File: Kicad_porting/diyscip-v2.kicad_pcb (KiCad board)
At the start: 2 copper layers, 86.4 x 24.1 mm, 30 parts, among them IC1 CD4051BE, IC2 CD4051BE, IC3 SN74HC595N, IC4 SN74HC595N, J1 Conn_01x05_Male, J3 Conn_01x05_Male, Q1 BSS138, Q2 BSS138, Q3 BSS138, U1 AMS1117-3.3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

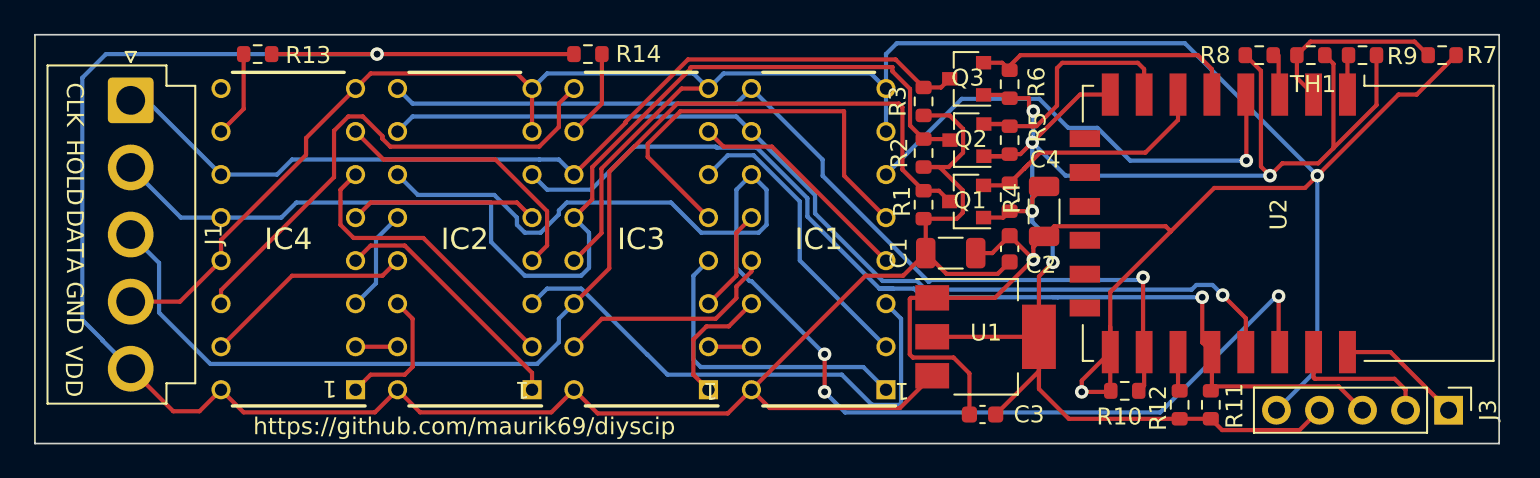
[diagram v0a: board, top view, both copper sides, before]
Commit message: gerber with thermal copper
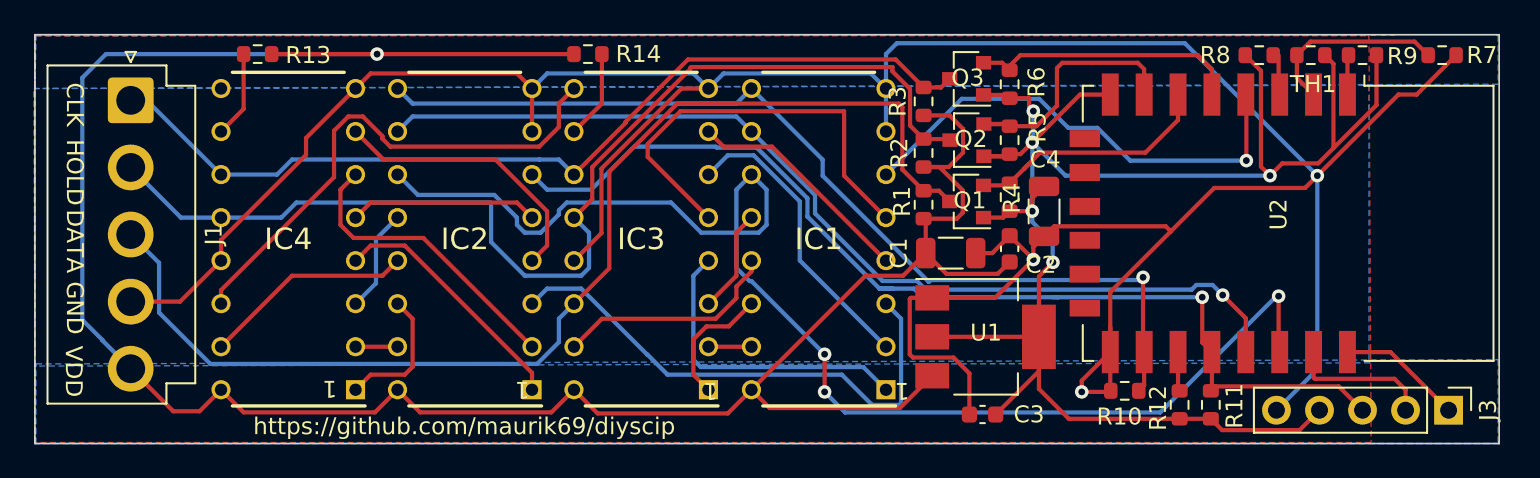
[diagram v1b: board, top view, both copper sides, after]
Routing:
- added copper zone on B.Cu, net GND
- added copper zone on F.Cu, net GND

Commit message: Correzione errore scritta connettore programmazione.
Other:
- board text added: "+3.3"
- board text removed: "3.3V"
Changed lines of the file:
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@@
   )
   (layers
-    (0 F.Cu signal)
-    (31 B.Cu signal)
+    (0 F.Cu signal hide)
+    (31 B.Cu signal hide)
     (32 B.Adhes user)
     (33 F.Adhes user)
@@
     (44 Edge.Cuts user)
     (45 Margin user)
-    (46 B.CrtYd user hide)
+    (46 B.CrtYd user)
     (47 F.CrtYd user)
-    (48 B.Fab user hide)
+    (48 B.Fab user)
     (49 F.Fab user hide)
   )
@@
       (effects (font (size 1 1) (thickness 0.15)))
     )
-    (fp_text value Conn_01x05_Male (at 0 12.49 90) (layer F.Fab)
+    (fp_text value Conn_01x05_Male (at 2.159 4.953 180) (layer F.Fab)
       (effects (font (size 1 1) (thickness 0.15)))
     )
@@
       (effects (font (size 1 1) (thickness 0.15)))
     )
-    (fp_text value "Thermistor NTC 10K" (at 0 1.43) (layer F.Fab)
+    (fp_text value "Thermistor NTC 10K" (at -0.191 3.1115) (layer F.Fab)
       (effects (font (size 1 1) (thickness 0.15)))
     )
@@
       (effects (font (size 1 1) (thickness 0.15)))
     )
-    (fp_text value 10k (at 0 1.43) (layer F.Fab)
+    (fp_text value 10k (at 0.1275 1.651) (layer F.Fab)
       (effects (font (size 1 1) (thickness 0.15)))
     )
@@
       (effects (font (size 1 1) (thickness 0.15)))
     )
-    (fp_text value ESP-12E (at -0.06 -12.78 90) (layer F.Fab)
+    (fp_text value ESP-12E (at 0.615 2.341 90) (layer F.Fab)
       (effects (font (size 1 1) (thickness 0.15)))
     )
@@
       (effects (font (size 1 1) (thickness 0.15)))
     )
-    (fp_text value 10K (at 0 1.43) (layer F.Fab)
+    (fp_text value 10K (at -0.1275 -1.778) (layer F.Fab)
       (effects (font (size 1 1) (thickness 0.15)))
     )
@@
       (effects (font (size 1 1) (thickness 0.15)))
     )
-    (fp_text value 10K (at 0 1.43) (layer F.Fab)
+    (fp_text value 10K (at 0.1275 1.8415) (layer F.Fab)
       (effects (font (size 1 1) (thickness 0.15)))
     )
@@
       (effects (font (size 1 1) (thickness 0.15)))
     )
-    (fp_text value 100nF (at 0 1.43) (layer F.Fab)
+    (fp_text value 100nF (at -0.013 -0.127) (layer F.Fab)
       (effects (font (size 1 1) (thickness 0.15)))
     )
@@
       (effects (font (size 1 1) (thickness 0.15)))
     )
-    (fp_text value AMS1117-3.3 (at 0 4.5) (layer F.Fab)
+    (fp_text value AMS1117-3.3 (at 0.2155 -0.113) (layer F.Fab)
       (effects (font (size 1 1) (thickness 0.15)))
     )
@@
       (effects (font (size 1 1) (thickness 0.15)))
     )
-    (fp_text value BSS138 (at 0 2.5) (layer F.Fab)
+    (fp_text value BSS138 (at 0.143 0.061) (layer F.Fab)
       (effects (font (size 1 1) (thickness 0.15)))
     )
@@
       (effects (font (size 1 1) (thickness 0.15)))
     )
-    (fp_text value 100nF (at 0 1.43 90) (layer F.Fab)
+    (fp_text value 100nF (at -0.9525 1.27 180) (layer F.Fab)
       (effects (font (size 1 1) (thickness 0.15)))
     )
@@
     (fp_line (start -1.6 -0.8) (end 1.6 -0.8) (layer F.Fab) (width 0.1))
     (fp_line (start -1.6 0.8) (end -1.6 -0.8) (layer F.Fab) (width 0.1))
-    (fp_text user %R (at 0 0) (layer F.Fab)
+    (fp_text user %R (at 0.049 0.0635) (layer F.Fab)
       (effects (font (size 0.8 0.8) (thickness 0.12)))
     )
@@
     (effects (font (size 1 1) (thickness 0.15)))
   )
-  (gr_text 3.3V (at 185.928 102.616) (layer B.SilkS)
+  (gr_text GND (at 187.1345 102.0445 270) (layer B.SilkS)
     (effects (font (size 1 1) (thickness 0.15)) (justify mirror))
   )
-  (gr_text GND (at 189.23 102.616) (layer B.SilkS)
+  (gr_text +3.3 (at 189.738 101.7905 270) (layer B.SilkS)
     (effects (font (size 1 1) (thickness 0.15)) (justify mirror))
   )
-  (gr_text G0 (at 192.3415 102.616) (layer B.SilkS)
+  (gr_text G0 (at 192.278 102.5525 270) (layer B.SilkS)
     (effects (font (size 1 1) (thickness 0.15)) (justify mirror))
   )
-  (gr_text RX (at 194.945 102.616) (layer B.SilkS)
+  (gr_text RX (at 194.7545 102.616 270) (layer B.SilkS)
     (effects (font (size 1 1) (thickness 0.15)) (justify mirror))
   )
-  (gr_text TX (at 197.485 102.6795) (layer B.SilkS)
+  (gr_text TX (at 197.358 102.5525 270) (layer B.SilkS)
     (effects (font (size 1 1) (thickness 0.15)) (justify mirror))
   )

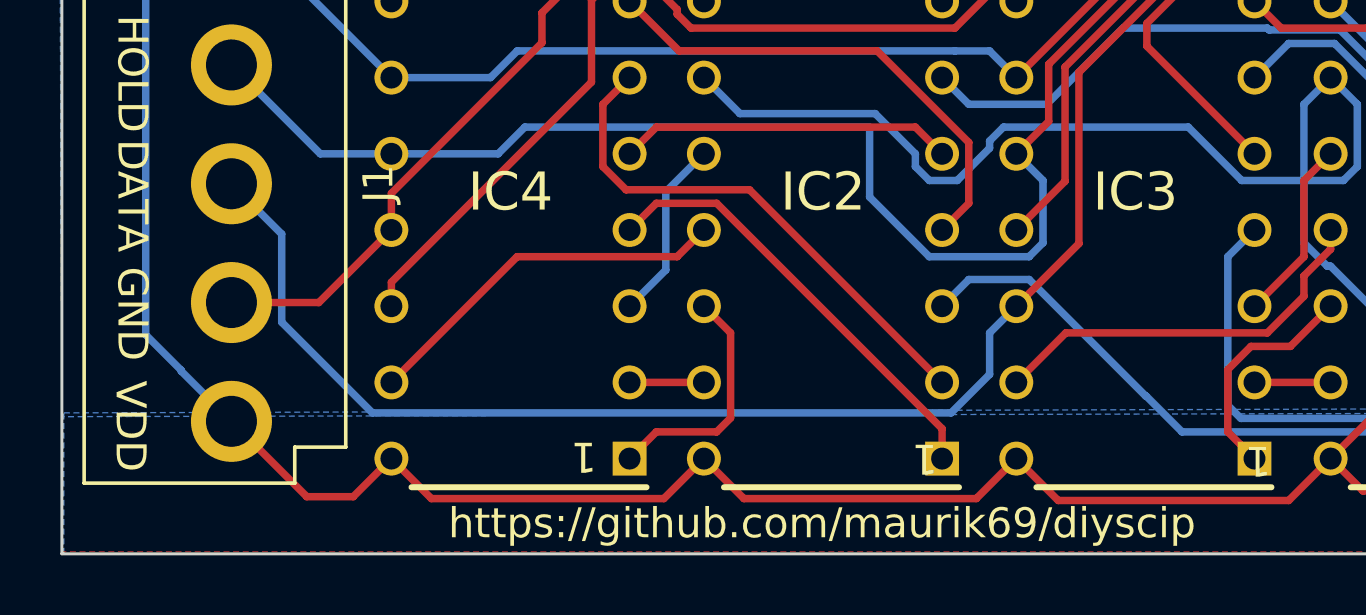
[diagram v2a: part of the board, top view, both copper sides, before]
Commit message: Aggiunta resistenza "dimenticata" su segnale DATA
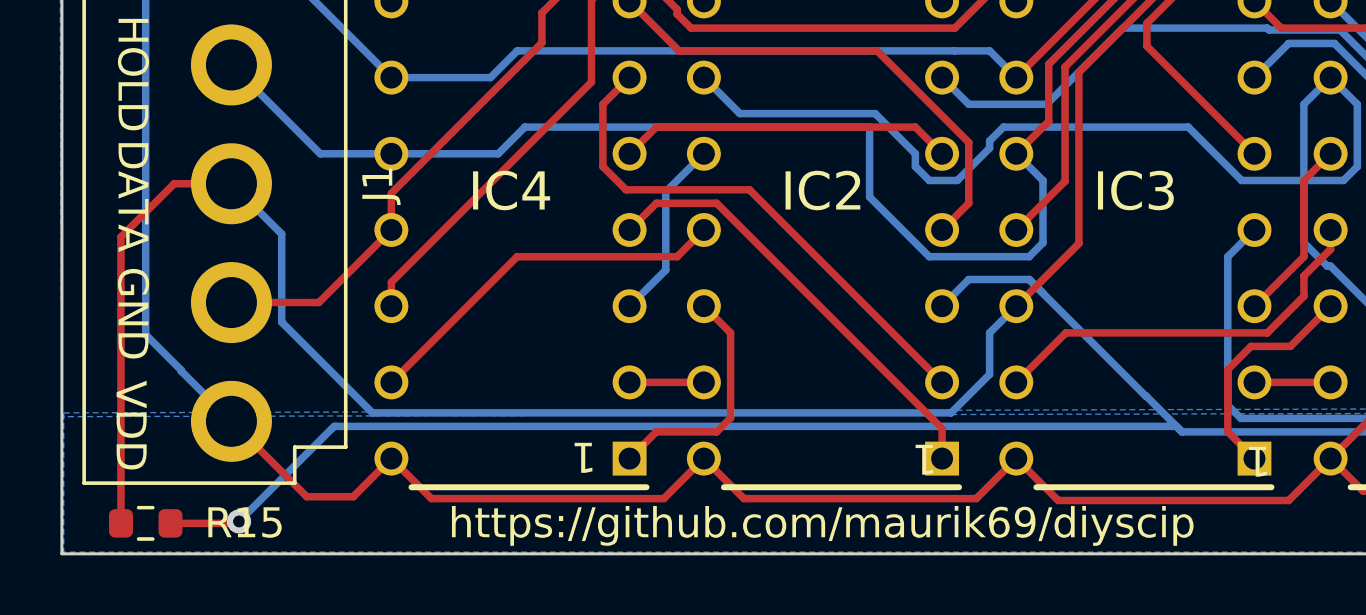
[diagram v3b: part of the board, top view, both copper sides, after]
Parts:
- added R15: 1K, Resistor_SMD:R_0603_1608Metric, F.Cu at (116.7, 105.9)
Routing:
- net Net-(IC1-Pad3): track 31.3 -> 67.3 mm, vias 0 -> 1
- net DATA_TTL: track 68.3 -> 82.3 mm
